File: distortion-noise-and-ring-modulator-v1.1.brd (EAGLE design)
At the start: 44.8 x 24.1 mm, 74 parts, among them IC1 TL074JT, IC4 LM13700SL, IC5 TL074JT, Q1 MMBT3906, T1 NOISE-2N3904, U1 MC1496DR2G, X2 MA06-1JC, X3 MA06-1JC

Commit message: Nude pin headers
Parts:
- X2, X3: value MA06-1JC -> MA06-1JN; device joakim:MA06-1J -> joakim:MA06N-1J
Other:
- board text added: "Nse"
- board text removed: "Lvl1"
- board text removed: "Lvl2"
- board text removed: "Noise"
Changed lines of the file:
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@@
 <layer number="14" name="Route14" color="1" fill="6" visible="no" active="no"/>
 <layer number="15" name="Route15" color="4" fill="6" visible="no" active="no"/>
-<layer number="16" name="Bottom" color="1" fill="1" visible="yes" active="yes"/>
+<layer number="16" name="Bottom" color="1" fill="1" visible="no" active="yes"/>
 <layer number="17" name="Pads" color="2" fill="1" visible="yes" active="yes"/>
 <layer number="18" name="Vias" color="2" fill="1" visible="yes" active="yes"/>
@@
 <layer number="20" name="Dimension" color="15" fill="1" visible="yes" active="yes"/>
 <layer number="21" name="tPlace" color="7" fill="1" visible="yes" active="yes"/>
-<layer number="22" name="bPlace" color="7" fill="1" visible="yes" active="yes"/>
+<layer number="22" name="bPlace" color="7" fill="1" visible="no" active="yes"/>
 <layer number="23" name="tOrigins" color="15" fill="1" visible="yes" active="yes"/>
-<layer number="24" name="bOrigins" color="15" fill="1" visible="yes" active="yes"/>
-<layer number="25" name="tNames" color="7" fill="1" visible="no" active="yes"/>
+<layer number="24" name="bOrigins" color="15" fill="1" visible="no" active="yes"/>
+<layer number="25" name="tNames" color="7" fill="1" visible="yes" active="yes"/>
 <layer number="26" name="bNames" color="7" fill="1" visible="no" active="yes"/>
 <layer number="27" name="tValues" color="7" fill="1" visible="no" active="yes"/>
@@
 <layer number="38" name="bTest" color="7" fill="1" visible="no" active="yes"/>
 <layer number="39" name="tKeepout" color="4" fill="11" visible="yes" active="yes"/>
-<layer number="40" name="bKeepout" color="1" fill="11" visible="yes" active="yes"/>
+<layer number="40" name="bKeepout" color="1" fill="11" visible="no" active="yes"/>
 <layer number="41" name="tRestrict" color="4" fill="10" visible="yes" active="yes"/>
-<layer number="42" name="bRestrict" color="1" fill="10" visible="yes" active="yes"/>
+<layer number="42" name="bRestrict" color="1" fill="10" visible="no" active="yes"/>
 <layer number="43" name="vRestrict" color="2" fill="10" visible="no" active="yes"/>
 <layer number="44" name="Drills" color="7" fill="1" visible="no" active="yes"/>
@@
 <layer number="50" name="dxf" color="7" fill="1" visible="no" active="no"/>
 <layer number="51" name="tDocu" color="7" fill="1" visible="yes" active="yes"/>
-<layer number="52" name="bDocu" color="7" fill="1" visible="yes" active="yes"/>
+<layer number="52" name="bDocu" color="7" fill="1" visible="no" active="yes"/>
 <layer number="53" name="tGND_GNDA" color="7" fill="9" visible="no" active="no"/>
 <layer number="54" name="bGND_GNDA" color="1" fill="9" visible="no" active="no"/>
@@
 <wire x1="0" y1="20.32" x2="0" y2="3.81" width="0" layer="20"/>
 <wire x1="0" y1="3.81" x2="1.27" y2="2.54" width="0" layer="20"/>
-<text x="13.335" y="17.78" size="1.27" layer="26" font="vector" rot="MR270">+12v</text>
-<text x="12.065" y="5.3975" size="1.27" layer="26" font="vector" rot="MR90">-12v</text>
+<text x="15.875" y="17.78" size="1.27" layer="26" font="vector" rot="MR270">+12v</text>
+<text x="14.605" y="5.3975" size="1.27" layer="26" font="vector" rot="MR90">-12v</text>
 <text x="20.955" y="17.78" size="1.27" layer="26" font="vector" rot="MR270">AGND</text>
 <text x="22.225" y="5.3975" size="1.27" layer="26" font="vector" rot="MR90">Sig</text>
@@
 distortion
 &amp; Noise</text>
-<text x="15.875" y="17.78" size="1.27" layer="26" font="vector" rot="MR270">White</text>
-<text x="18.415" y="17.78" size="1.27" layer="26" font="vector" rot="MR270">Pink</text>
+<text x="18.415" y="17.78" size="1.27" layer="26" font="vector" rot="MR270">White</text>
+<text x="17.145" y="5.3975" size="1.27" layer="26" font="vector" rot="MR90">Pink</text>
 <text x="19.685" y="5.3975" size="1.27" layer="26" font="vector" rot="MR90">Red</text>
-<text x="17.145" y="5.3975" size="1.27" layer="26" font="vector" rot="MR90">Lvl1</text>
-<text x="14.605" y="5.3975" size="1.27" layer="26" font="vector" rot="MR90">Lvl2</text>
 <text x="24.765" y="5.3975" size="1.27" layer="26" font="vector" rot="MR90">In</text>
 <text x="27.305" y="5.3975" size="1.27" layer="26" font="vector" rot="MR90">CV</text>
@@
 <text x="28.575" y="13.0175" size="1.27" layer="26" font="vector" rot="MR270">Dist</text>
 <wire x1="29.21" y1="20.0025" x2="29.21" y2="2.8575" width="0.127" layer="26"/>
-<wire x1="13.97" y1="20.0025" x2="13.97" y2="2.8575" width="0.127" layer="26"/>
+<wire x1="16.51" y1="20.0025" x2="16.51" y2="2.8575" width="0.127" layer="26"/>
 <wire x1="21.59" y1="2.8575" x2="21.59" y2="12.7" width="0.127" layer="26"/>
 <wire x1="21.59" y1="12.7" x2="21.59" y2="20.0025" width="0.127" layer="26"/>
 <wire x1="19.05" y1="20.0025" x2="19.05" y2="12.7" width="0.127" layer="26"/>
 <wire x1="19.05" y1="12.7" x2="21.59" y2="12.7" width="0.127" layer="26"/>
-<text x="14.9225" y="12.065" size="1.27" layer="26" font="vector" rot="MR180">Noise</text>
+<text x="17.4625" y="11.43" size="1.27" layer="26" font="vector" rot="MR180">Nse</text>
 <text x="22.5425" y="12.065" size="1.27" layer="26" font="vector" rot="MR180">RM</text>
-<wire x1="11.43" y1="20.0025" x2="11.43" y2="2.8575" width="0.127" layer="26"/>
+<wire x1="13.97" y1="20.0025" x2="13.97" y2="2.8575" width="0.127" layer="26"/>
 <text x="22.86" y="0" size="1.016" layer="25" font="vector">Signal
 trim</text>
@@
 <attribute name="VALUE" x="29.155" y="-2.045" size="1.27" layer="27"/>
 </element>
-<element name="X2" library="joakim" package="MA06-1J" value="MA06-1JC" x="21.59" y="3.81" smashed="yes">
+<element name="X2" library="joakim" package="MA06N-1J" value="MA06-1JN" x="21.59" y="3.81" smashed="yes">
 <attribute name="NAME" x="13.97" y="5.461" size="1.27" layer="25" ratio="10"/>
 <attribute name="VALUE" x="17.78" y="0.889" size="1.27" layer="27" ratio="10"/>
 </element>
-<element name="X3" library="joakim" package="MA06-1J" value="MA06-1JC" x="21.59" y="19.05" smashed="yes" rot="R180">
+<element name="X3" library="joakim" package="MA06N-1J" value="MA06-1JN" x="21.59" y="19.05" smashed="yes" rot="R180">
 <attribute name="NAME" x="29.21" y="17.399" size="1.27" layer="25" ratio="10" rot="R180"/>
 <attribute name="VALUE" x="25.4" y="21.971" size="1.27" layer="27" ratio="10" rot="R180"/>

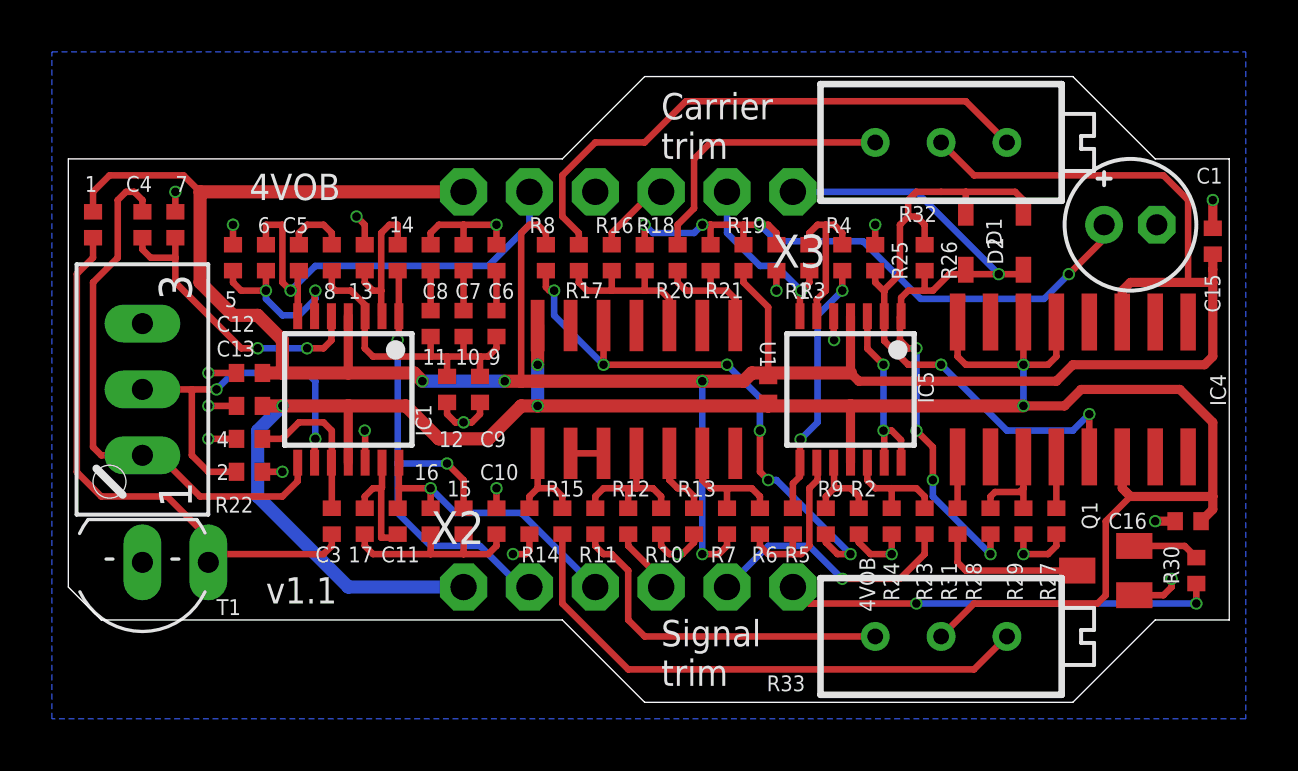
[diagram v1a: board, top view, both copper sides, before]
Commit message: Replaced 100uf electrolytic cap with two ceramic. Changed 200R to 500R pot to get a single extended part
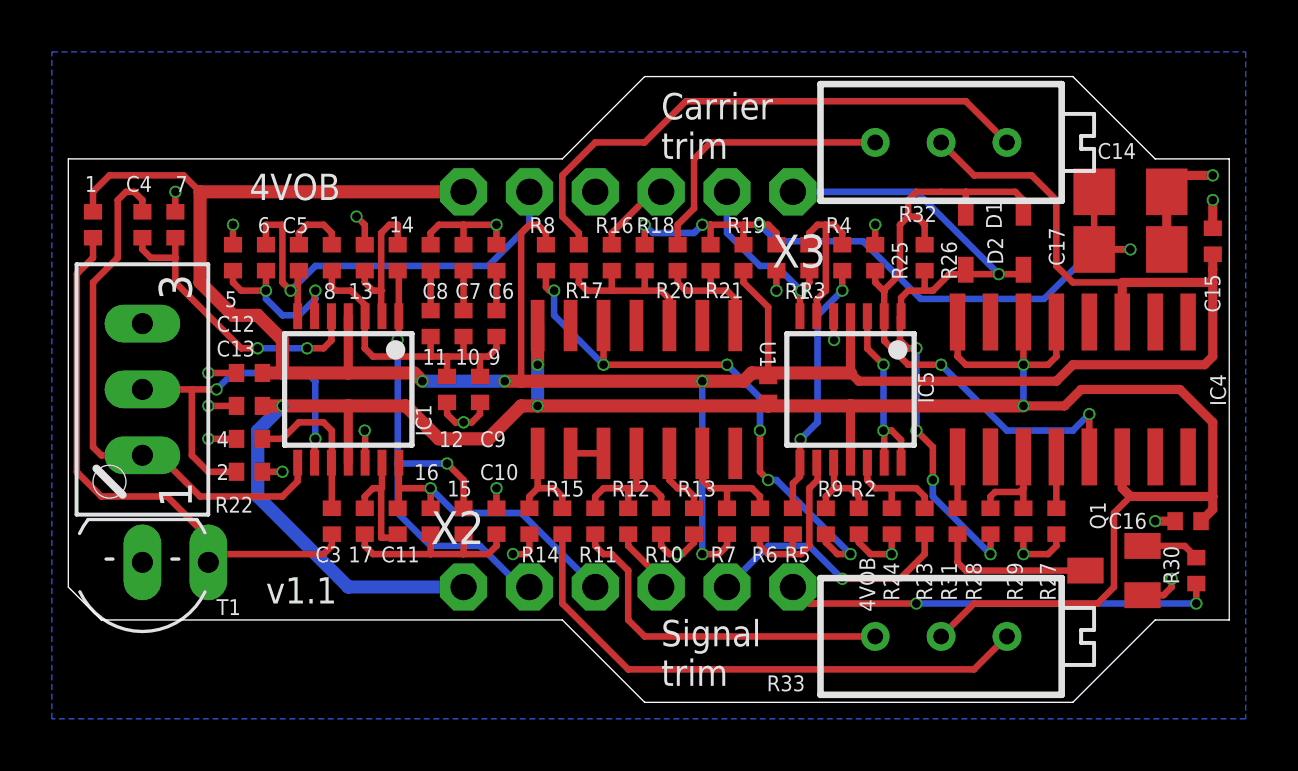
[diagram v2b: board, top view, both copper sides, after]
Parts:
- removed C1: 100u 25V, rcl:E2-5
- added C14, C17: 47uF, rcl:C1206
- R33: value 200R -> 500R
- moved Q1 0.32 mm to (40.3, 4.45)
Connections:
- net GND: now also C14.2, C17.2; no longer C1.-
- net N$9: now also C14.1, C17.1; no longer C1.+
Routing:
- net GND: track 31.0 -> 34.9 mm, vias 21 -> 22
- net N$9: track 24.2 -> 28.1 mm
- net +12V: track 108.7 -> 106.0 mm

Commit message: Changed to 3k3 on pink filter output to save cost with JLCPCB
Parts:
- 11: value 3k -> 3k3
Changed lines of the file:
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@@
 <attribute name="VALUE" x="17.145" y="13.335" size="1.27" layer="27" rot="R90"/>
 </element>
-<element name="11" library="rcl" library_urn="urn:adsk.eagle:library:334" package="R0402" package3d_urn="urn:adsk.eagle:package:23547/3" value="3k" x="13.97" y="13.97" smashed="yes" rot="R90">
+<element name="11" library="rcl" library_urn="urn:adsk.eagle:library:334" package="R0402" package3d_urn="urn:adsk.eagle:package:23547/3" value="3k3" x="13.97" y="13.97" smashed="yes" rot="R90">
 <attribute name="NAME" x="13.6525" y="12.3825" size="0.6096" layer="25" font="vector"/>
 <attribute name="POPULARITY" value="0" x="25.4" y="13.97" size="1.778" layer="27" rot="R90" display="off"/>
